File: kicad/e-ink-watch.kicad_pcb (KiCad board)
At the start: 4 copper layers, 40 x 40 mm, 42 parts, among them SW1 BTN1, SW2 BTN2, SW3 BTN3, U1 MDBT50Q-1MV2, U2 BQ25120A

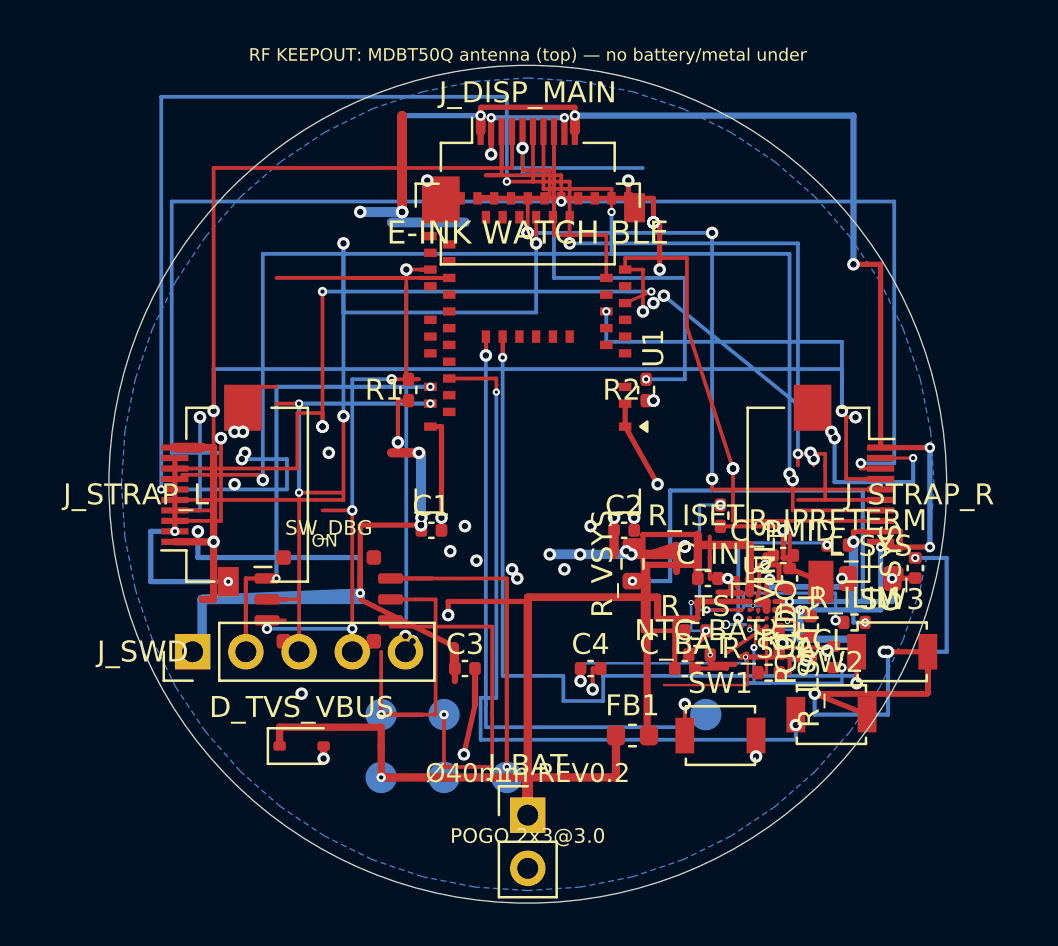
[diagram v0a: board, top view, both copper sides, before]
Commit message: Pass-AZ: hop SDA under VBAT with pour keepouts (unc 6→5).
Notch B GND, In1 GND, and In2 3V3 so the SDA vias can change layers under the VBAT bar. shorting_items stays 0. R_SCL and SW_DBG stay seated.

Co-authored-by: illiapliukhin <illiapliukhin@users.noreply.github.com>
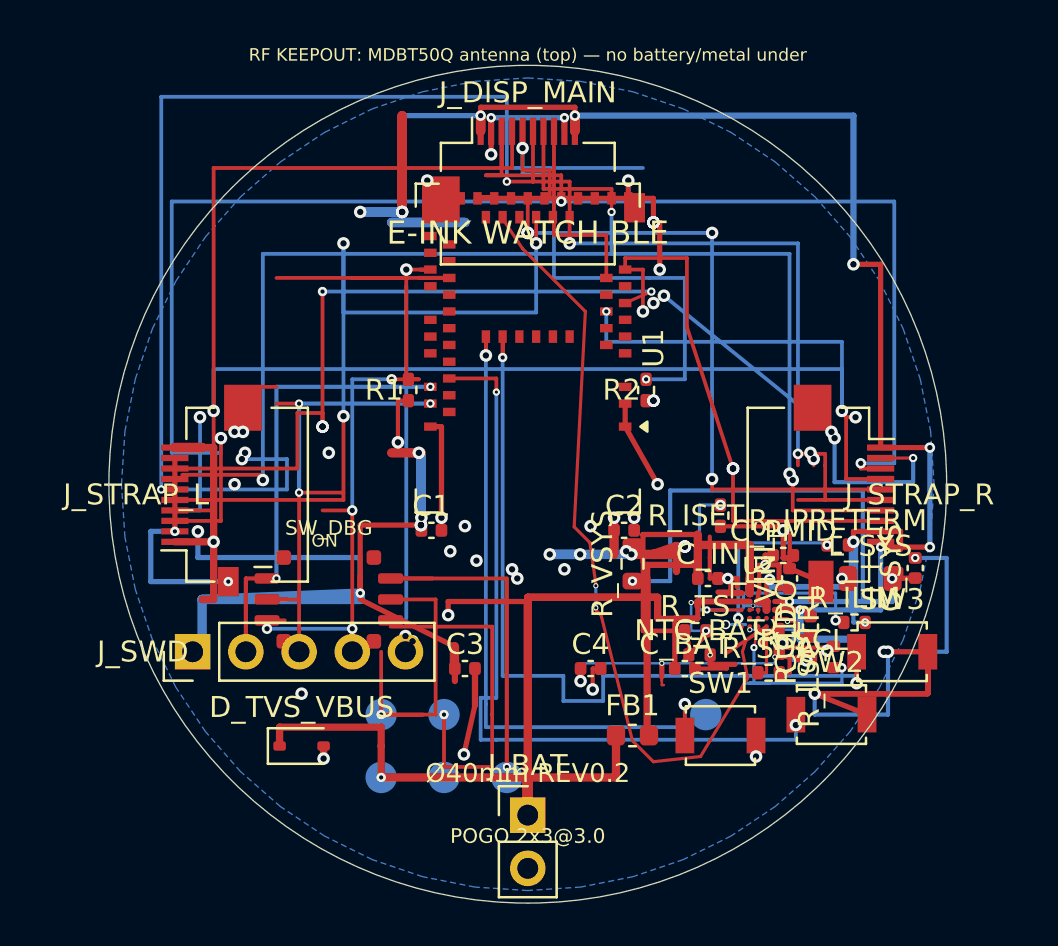
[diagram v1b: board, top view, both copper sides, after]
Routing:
- net SDA: track 4.96 -> 42.1 mm, vias 0 -> 2
- net 3V3: track 111.2 -> 107.2 mm, vias 26 -> 27
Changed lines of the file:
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@@
 	)
 	(segment
-		(start 110.16 108.25)
+		(start 111.8 108.25)
 		(end 112.16 108.25)
 		(width 0.25)
@@
 	)
 	(segment
-		(start 110.46 108.1)
-		(end 110.16 108.25)
+		(start 106.4 109.2)
+		(end 106.4 108.55)
 		(width 0.25)
 		(layer "F.Cu")
@@
 	(segment
 		(start 106.5 109.59)
-		(end 110.5 109.59)
+		(end 106.4 109.59)
 		(width 0.12)
 		(layer "F.Cu")
@@
 	)
 	(segment
-		(start 110.5 109.59)
-		(end 110.5 108.25)
+		(start 106.4 109.59)
+		(end 106.4 108.55)
 		(width 0.12)
 		(layer "F.Cu")
@@
 	)
 	(segment
-		(start 110.5 108.25)
-		(end 110.16 108.25)
+		(start 106.4 109.4)
+		(end 106.4 108.9)
 		(width 0.12)
 		(layer "F.Cu")
@@
 	)
 	(via
-		(at 110.4 108.25)
+		(at 111.8 108.25)
 		(size 0.25)
 		(drill 0.15)
@@
 	)
 	(segment
-		(start 110.4 108.25)
-		(end 110.4 108.55)
+		(start 111.8 108.25)
+		(end 111.8 108.55)
 		(width 0.12)
 		(layer "B.Cu")
@@
 		(net 25)
 	)
+	(segment
+		(start 110.42 107.45)
+		(end 110.25 108.0)
+		(width 0.15)
+		(layer "F.Cu")
+		(net 27)
+	)
+	(segment
+		(start 110.25 108.0)
+		(end 110.5 109.25)
+		(width 0.15)
+		(layer "F.Cu")
+		(net 27)
+	)
+	(segment
+		(start 110.5 109.25)
+		(end 108.25 113.0)
+		(width 0.15)
+		(layer "F.Cu")
+		(net 27)
+	)
+	(segment
+		(start 108.25 113.0)
+		(end 106.0 113.25)
+		(width 0.15)
+		(layer "F.Cu")
+		(net 27)
+	)
+	(segment
+		(start 106.0 113.25)
+		(end 105.0 112.25)
+		(width 0.15)
+		(layer "F.Cu")
+		(net 27)
+	)
+	(segment
+		(start 105.0 112.25)
+		(end 103.5 106.25)
+		(width 0.15)
+		(layer "F.Cu")
+		(net 27)
+	)
+	(segment
+		(start 103.5 106.25)
+		(end 103.25 106.0)
+		(width 0.15)
+		(layer "F.Cu")
+		(net 27)
+	)
+	(segment
+		(start 103.25 106.0)
+		(end 103.25 105.9)
+		(width 0.15)
+		(layer "F.Cu")
+		(net 27)
+	)
+	(segment
+		(start 103.25 104.85)
+		(end 103.25 104.75)
+		(width 0.15)
+		(layer "F.Cu")
+		(net 27)
+	)
+	(segment
+		(start 103.25 104.75)
+		(end 102.965 102.785)
+		(width 0.15)
+		(layer "F.Cu")
+		(net 27)
+	)
+	(segment
+		(start 102.965 102.785)
+		(end 102.215 102.035)
+		(width 0.15)
+		(layer "F.Cu")
+		(net 27)
+	)
+	(segment
+		(start 102.215 102.035)
+		(end 102.75 91.75)
+		(width 0.15)
+		(layer "F.Cu")
+		(net 27)
+	)
+	(segment
+		(start 102.75 91.75)
+		(end 99.75 88.75)
+		(width 0.15)
+		(layer "F.Cu")
+		(net 27)
+	)
+	(segment
+		(start 99.75 88.75)
+		(end 98.75 87.25)
+		(width 0.15)
+		(layer "F.Cu")
+		(net 27)
+	)
+	(segment
+		(start 98.75 87.25)
+		(end 98.8 87.25)
+		(width 0.15)
+		(layer "F.Cu")
+		(net 27)
+	)
+	(segment
+		(start 103.25 105.9)
+		(end 103.25 104.85)
+		(width 0.15)
+		(layer "B.Cu")
+		(net 27)
+	)
+	(segment
+		(start 111.8 108.55)
+		(end 110.4 108.55)
+		(width 0.12)
+		(layer "B.Cu")
+		(net 2)
+	)
+	(via
+		(at 103.25 105.9)
+		(size 0.25)
+		(drill 0.15)
+		(layers "F.Cu" "B.Cu")
+		(net 27)
+	)
+	(via
+		(at 103.25 104.85)
+		(size 0.25)
+		(drill 0.15)
+		(layers "F.Cu" "B.Cu")
+		(net 27)
+	)
+	(via
+		(at 106.4 108.55)
+		(size 0.25)
+		(drill 0.15)
+		(layers "F.Cu" "B.Cu")
+		(net 2)
+	)
 	(via

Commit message: Pass-BA: stitch east–west 3V3_DISP with pour keepouts (unc 5→4).
SCL still has no exit from the R_SCL seat. The first clear route is a 0.28 mm 3V3_DISP hop inside x=85. shorting_items stays 0.

Co-authored-by: illiapliukhin <illiapliukhin@users.noreply.github.com>
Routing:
- net 3V3_DISP: track 103.6 -> 128.7 mm, vias 13 -> 17
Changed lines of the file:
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@@
 		(net 2)
+	)
+	(segment
+		(start 85.0 102.75)
+		(end 88.6 101.25)
+		(width 0.28)
+		(layer "F.Cu")
+		(net 3)
+	)
+	(segment
+		(start 92.2 96.75)
+		(end 90.7 92.25)
+		(width 0.28)
+		(layer "F.Cu")
+		(net 3)
+	)
+	(segment
+		(start 89.2 89.55)
+		(end 91.0 87.4)
+		(width 0.28)
+		(layer "F.Cu")
+		(net 3)
+	)
+	(segment
+		(start 91.0 87.4)
+		(end 92.0 87.0)
+		(width 0.28)
+		(layer "F.Cu")
+		(net 3)
+	)
+	(segment
+		(start 88.6 101.25)
+		(end 91.9 102.05)
+		(width 0.28)
+		(layer "B.Cu")
+		(net 3)
+	)
+	(segment
+		(start 91.9 102.05)
+		(end 92.2 101.55)
+		(width 0.28)
+		(layer "B.Cu")
+		(net 3)
+	)
+	(segment
+		(start 92.2 101.55)
+		(end 92.2 96.75)
+		(width 0.28)
+		(layer "B.Cu")
+		(net 3)
+	)
+	(segment
+		(start 90.7 92.25)
+		(end 88.6 90.15)
+		(width 0.28)
+		(layer "B.Cu")
+		(net 3)
+	)
+	(segment
+		(start 88.6 90.15)
+		(end 89.2 89.55)
+		(width 0.28)
+		(layer "B.Cu")
+		(net 3)
+	)
+	(via
+		(at 88.6 101.25)
+		(size 0.45)
+		(drill 0.2)
+		(layers "F.Cu" "B.Cu")
+		(net 3)
+	)
+	(via
+		(at 92.2 96.75)
+		(size 0.45)
+		(drill 0.2)
+		(layers "F.Cu" "B.Cu")
+		(net 3)
+	)
+	(via
+		(at 90.7 92.25)
+		(size 0.45)
+		(drill 0.2)
+		(layers "F.Cu" "B.Cu")
+		(net 3)
+	)
+	(via
+		(at 89.2 89.55)
+		(size 0.45)
+		(drill 0.2)
+		(layers "F.Cu" "B.Cu")
+		(net 3)
 	)
 	(via

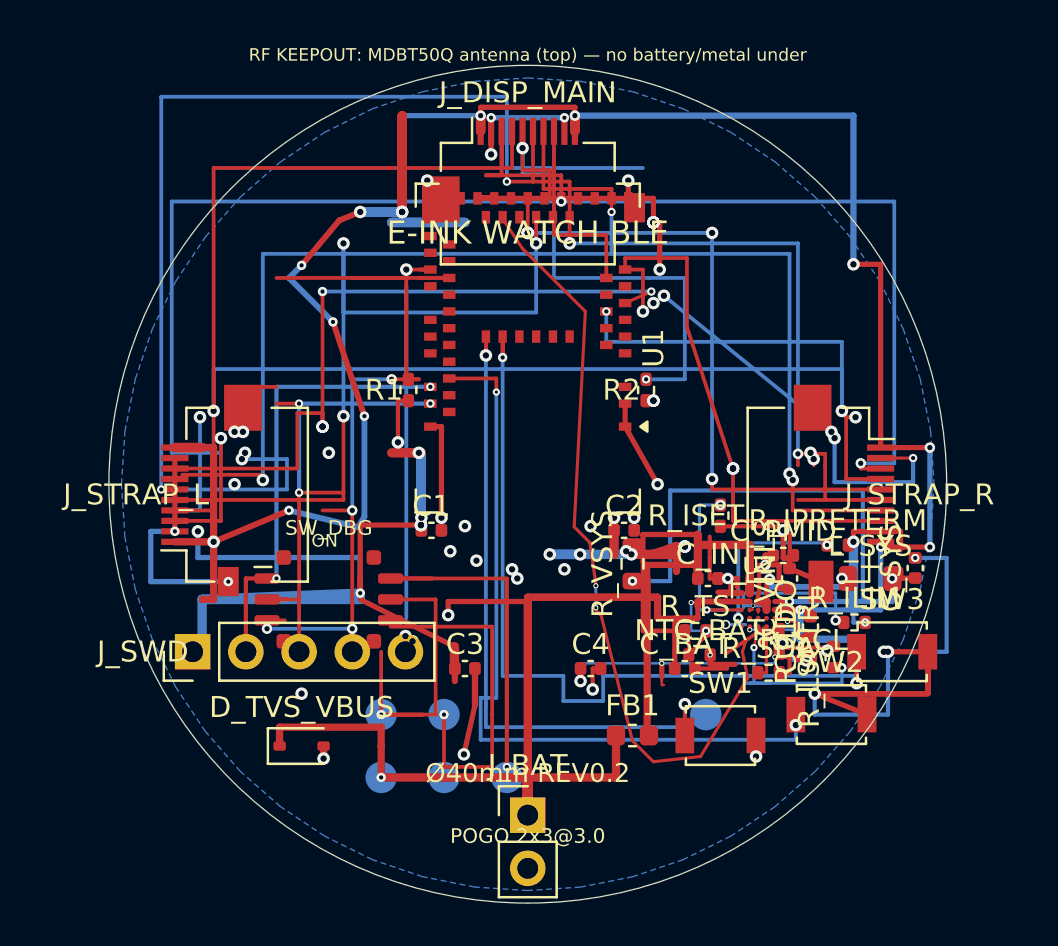
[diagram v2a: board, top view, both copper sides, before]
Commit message: Pass-BD: hop SDA under EPD_RST so I2C meets (unc 3, shorting 0).
Move R_SCL and R_SDA, bow the EPD_RST wall, and notch only the fill holes the two SDA vias drill. A5, PMIC_INT, and TS stay open on a standard through-via board.

Co-authored-by: illiapliukhin <illiapliukhin@users.noreply.github.com>
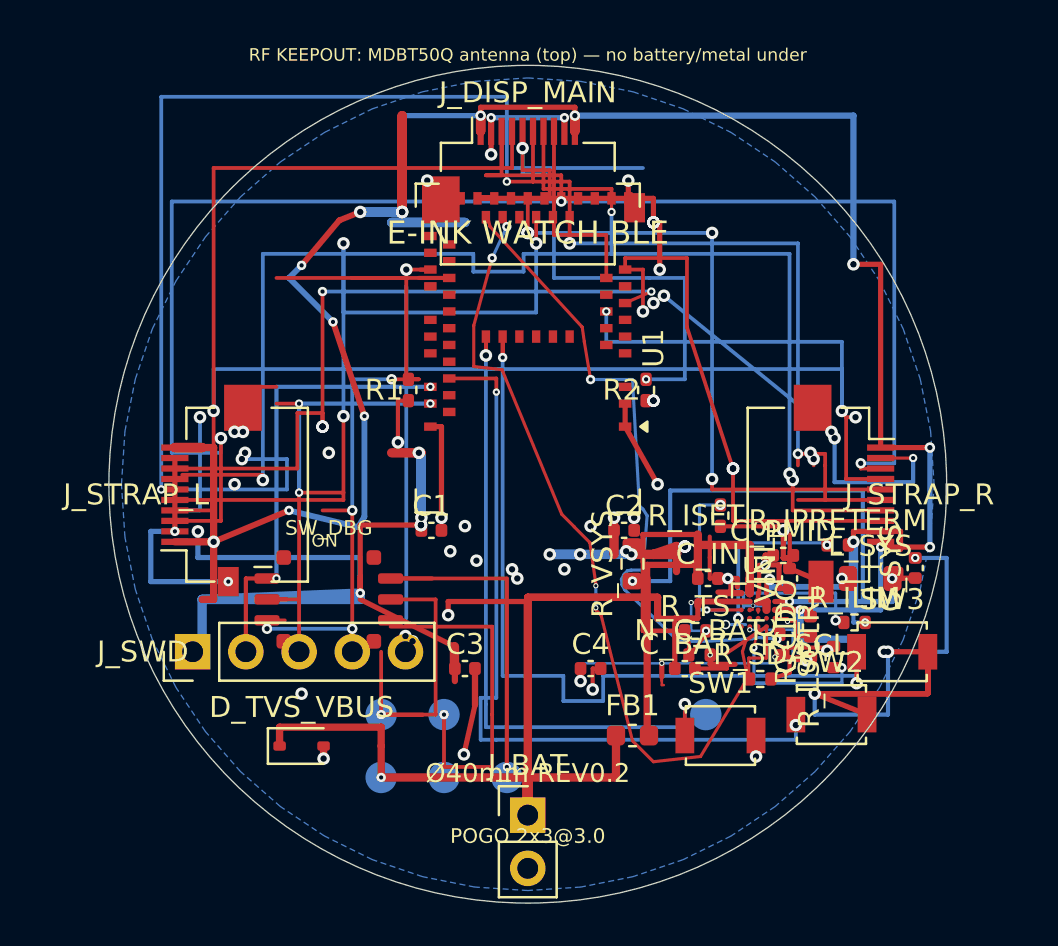
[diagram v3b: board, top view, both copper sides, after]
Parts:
- moved R_SDA 0.50 mm to (111.1, 109.3)
- moved R_SCL 0.23 mm to (112.0, 107.7)
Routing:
- net SCL: track 1.04 -> 31.5 mm, vias 0 -> 2
- net EPD_RST: track 65.2 -> 66.9 mm
- net SDA: track 42.1 -> 43.5 mm, vias 2 -> 4
- net 3V3: track 107.2 -> 107.5 mm, vias 27 -> 26

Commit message: Pass-BF: place BQ25619 with a 3.3 V LDO and display switch.
U2 moves to a WQFN-24 at rotation 0 so 0.50 mm pads do not overlap. SYS feeds an MCP1700 for 3V3, and a P-MOS makes 3V3_DISP. shorting stays 0; the new pads are not all tied (unc 3→30).

Co-authored-by: illiapliukhin <illiapliukhin@users.noreply.github.com>
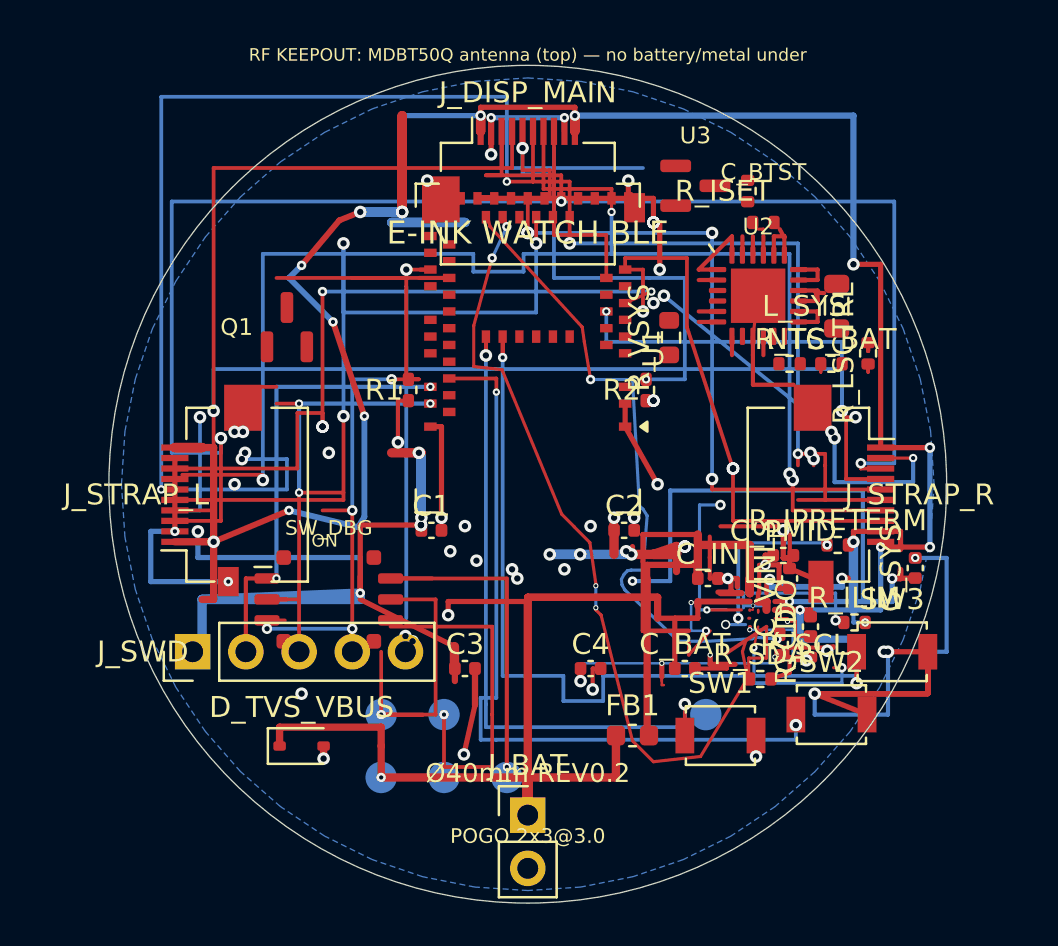
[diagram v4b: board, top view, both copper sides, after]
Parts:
- added C_BTST: 47nF, Resistor_SMD:R_0402_1005Metric, F.Cu at (111.2, 87.5)
- added Q1: DMG2305UX, EInkWatch:SOT-23, F.Cu at (88.5, 92.5)
- added U3: MCP1700-3302, EInkWatch:SOT-23, F.Cu at (108.0, 85.8)
- R_ISET: value 4.02k -> 10k
- R_LSCTRL: value 10k -> 100k
- R_VSYS: value 0R -> 4.7uF
- U2: value BQ25120A -> BQ25619; footprint EInkWatch:Texas_YFP0025_DSBGA-25_2.5x2.5mm_Layout5x5_P0.4mm -> EInkWatch:BQ25619_RTW_WQFN-24_4x4mm_P0.5mm
- moved R_ISET 15.6 mm to (110.5, 86.0)
- moved NTC_BAT 15.3 mm to (114.5, 94.2)
- moved U2 15.0 mm to (111.0, 91.0)
- moved R_LSCTRL 14.6 mm to (116.2, 93.8)
- moved R_TS 13.5 mm to (112.5, 94.2)
- moved L_SYS 13.1 mm to (114.8, 91.5), turned to 90 degrees
- moved R_VSYS 10.9 mm to (106.8, 93.0)
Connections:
- R_ISET pad 1: GND -> REGN
- R_ISET pad 2: ISET -> PSEL
- R_LSCTRL pad 1: LSCTRL -> DISP_EN
- R_TS pad 1: VBUS -> REGN
- R_VSYS pad 1: VSYS -> REGN
- R_VSYS pad 2: 3V3 -> GND
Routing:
- net GND: track 141.2 -> 149.7 mm
- net VBUS: track 29.1 -> 33.1 mm
- net VBAT: track 41.1 -> 44.3 mm
- net VSYS: track 29.2 -> 32.4 mm
- net SW: track 5.29 -> 8.10 mm
- net BTST: track 0.00 -> 1.48 mm
- net SDA: track 43.5 -> 44.4 mm
- net SCL: track 31.5 -> 32.4 mm
- net REGN: track 0.00 -> 0.90 mm
- net PSEL: track 0.00 -> 0.90 mm
- net PMID: track 6.00 -> 6.90 mm
- net PMIC_INT: track 18.3 -> 19.2 mm
- net 3V3_DISP: track 128.7 -> 129.5 mm
- net TS: track 7.16 -> 7.96 mm
- net 3V3: track 107.5 -> 108.3 mm
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
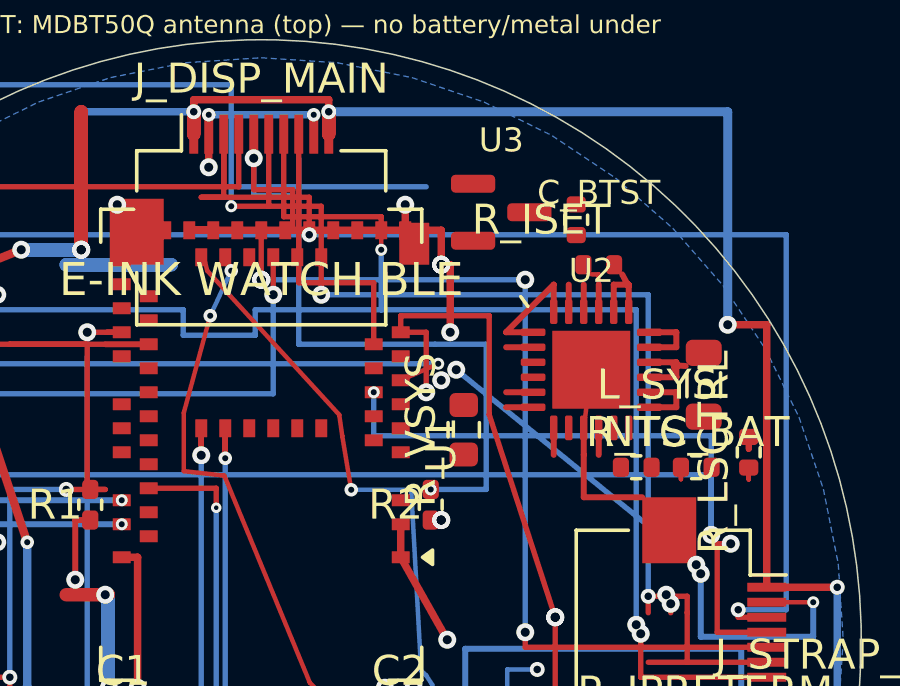
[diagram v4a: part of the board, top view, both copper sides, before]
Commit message: Pass-BG: fan out BQ25619 power and TS without a short.
Retract the 3V3 track off U1 pad 15 and tie the module rail into the In2 pour. Unconnected drops from 30 to 22 with shorting_items still 0.

Co-authored-by: illiapliukhin <illiapliukhin@users.noreply.github.com>
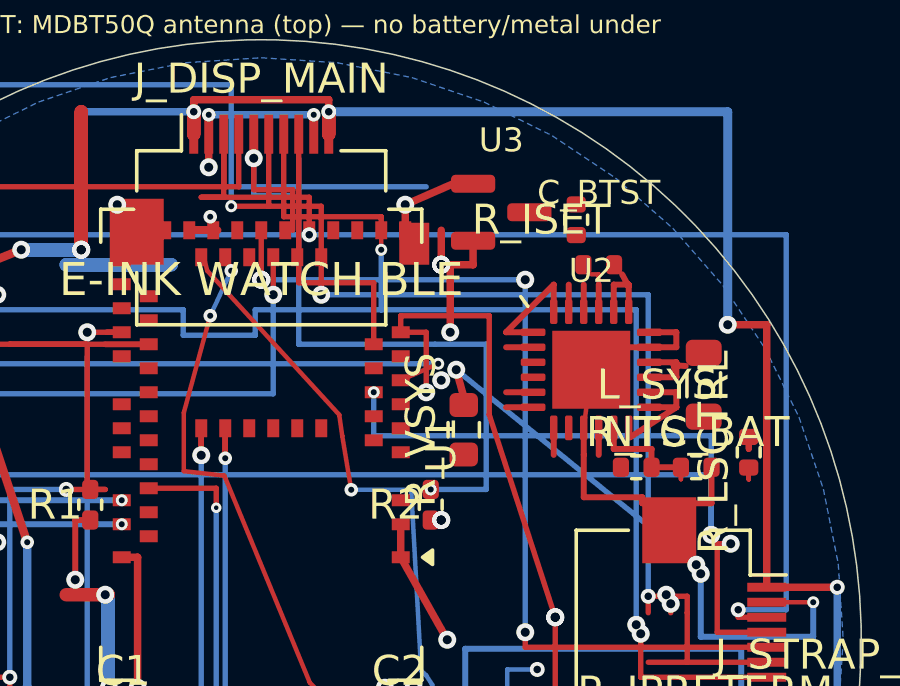
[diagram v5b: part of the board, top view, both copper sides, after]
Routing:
- net GND: track 149.7 -> 156.6 mm
- net TS: track 7.96 -> 11.5 mm
- net 3V3: track 108.3 -> 105.3 mm, vias 26 -> 27
- net VBAT: track 44.3 -> 46.2 mm
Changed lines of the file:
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@@
 	(segment
 		(start 97.6 86.35)
-		(end 106.0 86.35)
+		(end 98.55 86.35)
 		(width 0.25)
 		(layer "F.Cu")
@@
 		(net 3)
 	)
-	(via
+	(segment
+		(start 98.3 85.9)
+		(end 98.4 86.35)
+		(width 0.2)
+		(layer "F.Cu")
+		(net 2)
+	)
+	(segment
+		(start 98.3 85.9)
+		(end 98.5 88.3)
+		(width 0.25)
+		(layer "In2.Cu")
+		(net 2)
+	)
+	(segment
+		(start 112.6 90.25)
+		(end 112.1 90.25)
+		(width 0.2)
+		(layer "F.Cu")
+		(net 1)
+	)
+	(segment
+		(start 107.062 86.7)
+		(end 107.062 87.5)
+		(width 0.25)
+		(layer "F.Cu")
+		(net 2)
+	)
+	(segment
+		(start 107.062 87.5)
+		(end 106.3 87.5)
+		(width 0.25)
+		(layer "F.Cu")
+		(net 2)
+	)
+	(segment
+		(start 111.75 92.938)
+		(end 111.75 93.64)
+		(width 0.2)
+		(layer "F.Cu")
+		(net 31)
+	)
+	(segment
+		(start 111.75 93.64)
+		(end 113.01 93.64)
+		(width 0.2)
+		(layer "F.Cu")
+		(net 31)
+	)
+	(segment
+		(start 113.01 93.64)
+		(end 113.01 94.25)
+		(width 0.2)
+		(layer "F.Cu")
+		(net 31)
+	)
+	(segment
+		(start 113.01 94.25)
+		(end 113.99 94.25)
+		(width 0.2)
+		(layer "F.Cu")
+		(net 31)
+	)
+	(via
+		(at 98.3 85.9)
+		(size 0.45)
+		(drill 0.2)
+		(layers "F.Cu" "B.Cu")
+		(net 2)
+	)
+	(segment
+		(start 106.4 84.8)
+		(end 104.8 85.5)
+		(width 0.25)
+		(layer "F.Cu")
+		(net 1)
+	)
+	(segment
+		(start 106.75 91.9)
+		(end 106.5 91.0)
+		(width 0.25)
+		(layer "F.Cu")
+		(net 1)
+	)
+	(segment
+		(start 115.01 94.25)
+		(end 115.01 95.45)
+		(width 0.2)
+		(layer "F.Cu")
+		(net 1)
+	)
+	(segment
+		(start 115.01 95.45)
+		(end 112.7 95.45)
+		(width 0.2)
+		(layer "F.Cu")
+		(net 1)
+	)
+	(segment
+		(start 112.7 95.45)
+		(end 112.7 95.25)
+		(width 0.2)
+		(layer "F.Cu")
+		(net 1)
+	)
+	(segment
+		(start 112.3 93.25)
+		(end 113.84 92.25)
+		(width 0.2)
+		(layer "F.Cu")
+		(net 4)
+	)
+	(via
